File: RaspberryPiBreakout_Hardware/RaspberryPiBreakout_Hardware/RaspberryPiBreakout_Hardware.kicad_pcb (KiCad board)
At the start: 2 copper layers, 124.5 x 79.2 mm, 28 parts, among them U1 OKI, U2 Raspberry_Pi, U3 OKI

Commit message: layout and schematic changes
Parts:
- removed C2: 10u, Capacitor_SMD:C_0603_1608Metric_Pad1.05x0.95mm_HandSolder
- removed D2: LED, Diode_SMD:D_0603_1608Metric_Pad1.05x0.95mm_HandSolder
- removed G***: LOGO, MRDT_Silkscreens:0_MRDT_Logo_20mm
- removed R2: 500, Resistor_SMD:R_0603_1608Metric_Pad1.05x0.95mm_HandSolder
- removed U1: OKI, MRDT_Devices:OKI_Horizontal
- moved D1 3.81 mm to (156.4, 95.2)
- moved R1 3.81 mm to (151.4, 95.2)
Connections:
- U2 pad 2: +5V -> (no net)
- U2 pad 4: +5V -> (no net)
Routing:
- net +5V: track 57.5 -> 0.00 mm
- net +12V: track 98.4 -> 67.3 mm, vias 2 -> 0
- net SDA1: track 130.0 -> 135.0 mm, vias 6 -> 4
- net SCL1: track 117.5 -> 122.2 mm, vias 4 -> 5
- net Net-(D2-Pad2): track 3.17 -> 0.00 mm
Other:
- board text added: "3V3"
- board text added: "Raspberry Pi Breakout, Rev 1 Mars Rover Design Team Missouri S&T, 2020 Zak Brooks"
- board text added: "Rx"
- board text added: "Tx"
- board text removed: "5v"
- board text removed: "Raspberry Pi Breakout, Rev 2 Mars Rover Design Team Missouri S&T, 2019 Zak Brooks"

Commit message: finished updating layout
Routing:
- net +12V: track 67.3 -> 98.4 mm
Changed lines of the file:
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@@
     (thickness 1.6)
     (drawings 40)
-    (tracks 83)
+    (tracks 86)
     (zones 0)
     (modules 23)
@@
   (segment (start 112.395 102.87) (end 112.395 106.045) (width 0.762) (layer F.Cu) (net 2))
   (segment (start 112.395 102.87) (end 112.395 88.9) (width 0.762) (layer F.Cu) (net 2))
-  (segment (start 119.38 91.44) (end 119.38 106.045) (width 0.762) (layer F.Cu) (net 2))
   (segment (start 119.38 88.9) (end 119.38 91.44) (width 0.762) (layer F.Cu) (net 2))
+  (segment (start 149.87 95.25) (end 119.38 95.25) (width 0.381) (layer F.Cu) (net 2))
+  (segment (start 150.495 95.25) (end 149.87 95.25) (width 0.381) (layer F.Cu) (net 2))
+  (segment (start 119.38 91.44) (end 119.38 95.25) (width 0.762) (layer F.Cu) (net 2))
+  (segment (start 119.38 95.25) (end 119.38 106.045) (width 0.762) (layer F.Cu) (net 2))
   (segment (start 107.315 102.87) (end 107.315 106.045) (width 0.762) (layer F.Cu) (net 3))
   (segment (start 107.315 78.74) (end 107.315 83.185) (width 0.762) (layer B.Cu) (net 3))

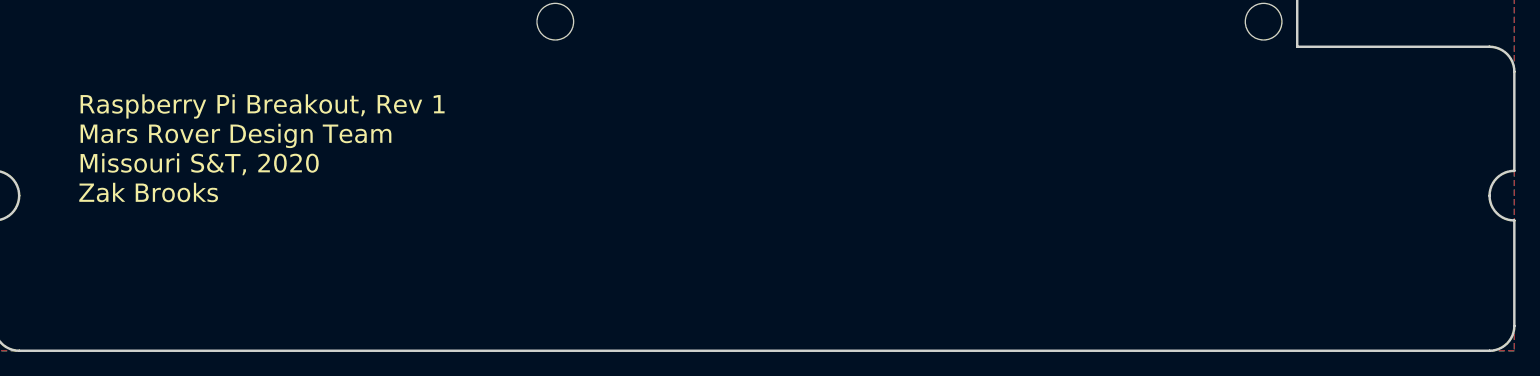
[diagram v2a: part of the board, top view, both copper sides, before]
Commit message: Added silkscreens
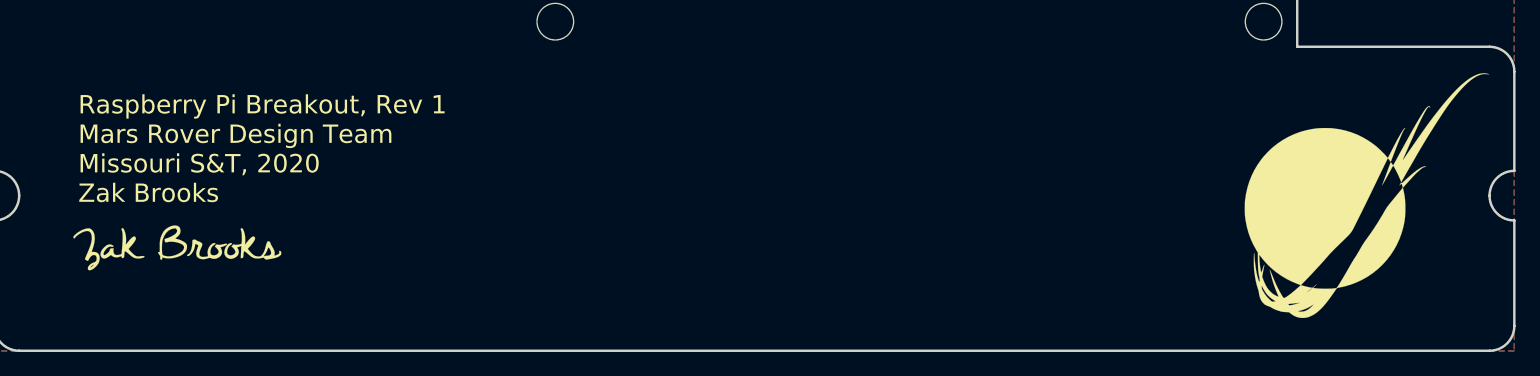
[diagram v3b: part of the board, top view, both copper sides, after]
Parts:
- added G***: LOGO, MRDT_Silkscreens:z_sig_ZakBrooks_sig15mm, F.Cu at (87.0, 145.4)
- added G***: LOGO, MRDT_Silkscreens:0_MRDT_Logo_20mm, F.Cu at (184.8, 141.0)
- added G***: LOGO, MRDT_Silkscreens:2_Dahlbot_2.0, B.Cu at (182.9, 142.2)

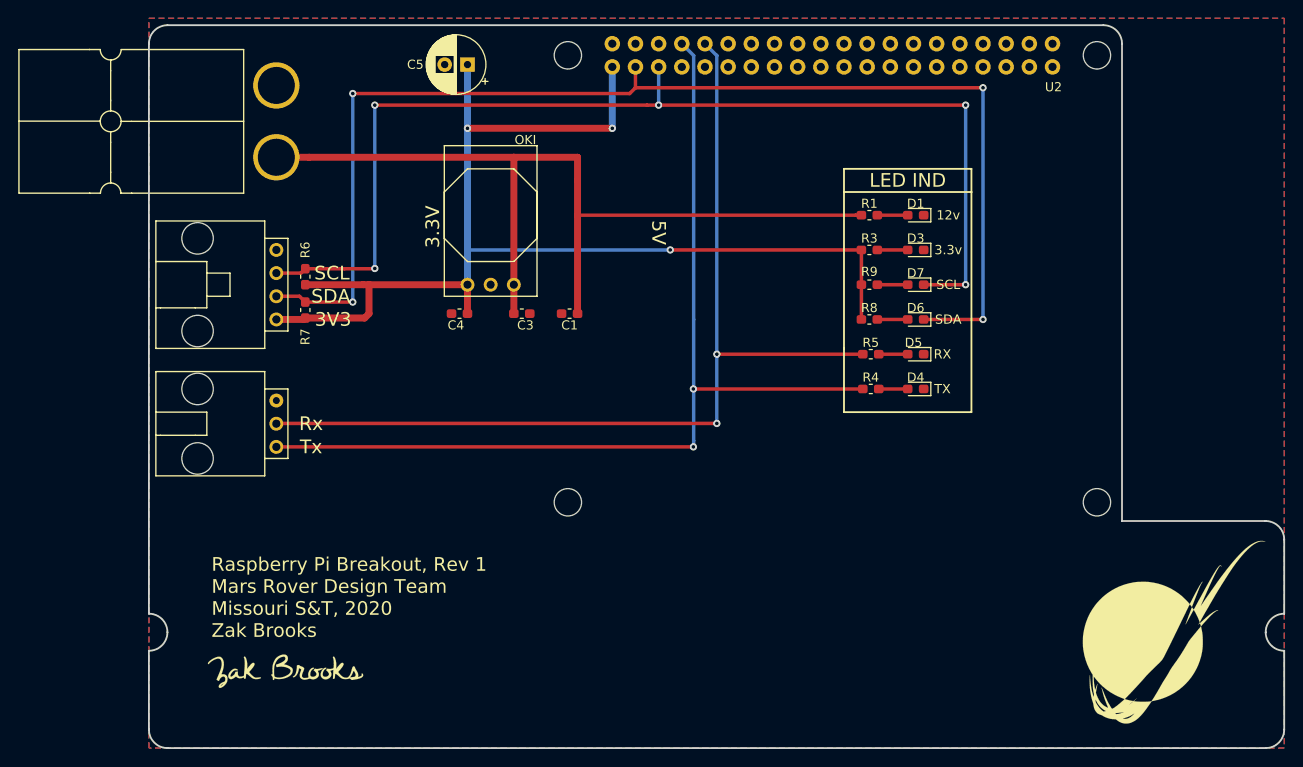
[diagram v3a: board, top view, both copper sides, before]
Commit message: Added 5v OKI back to the layout
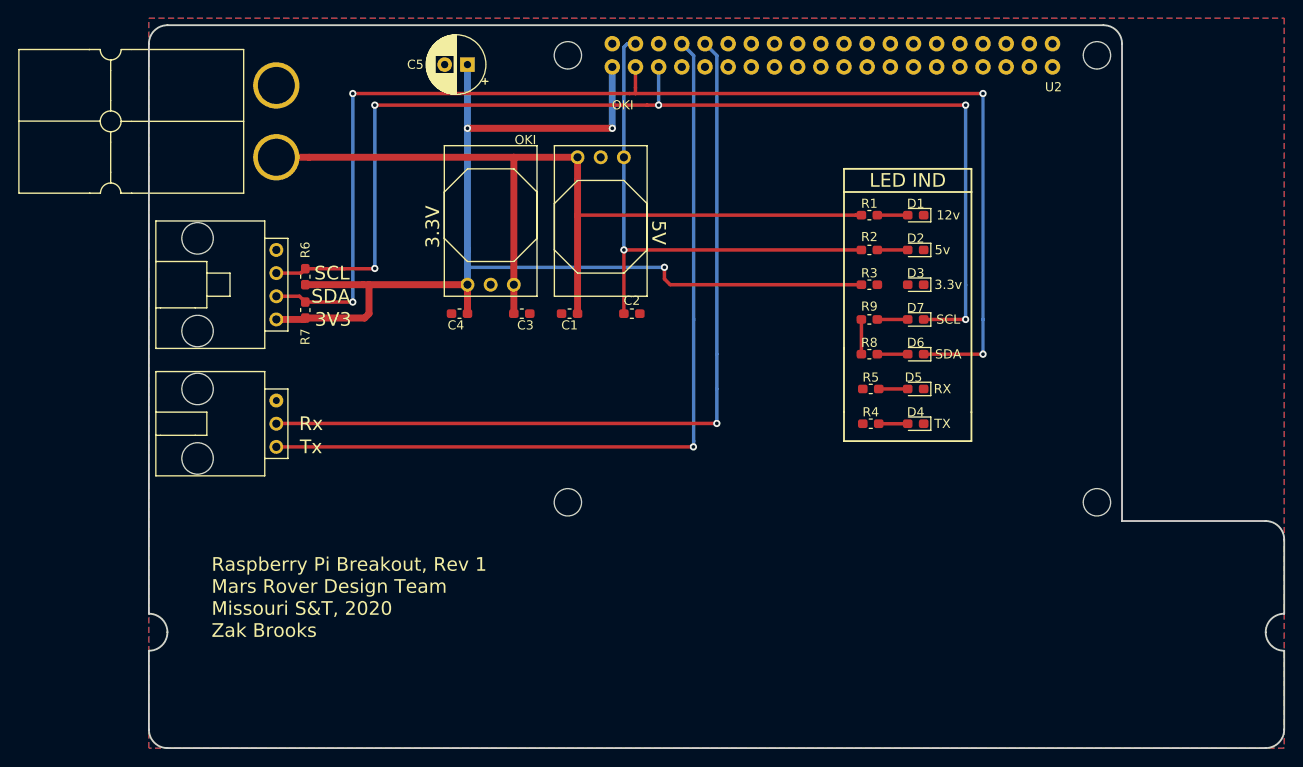
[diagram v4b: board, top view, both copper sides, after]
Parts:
- removed G***: LOGO, MRDT_Silkscreens:z_sig_ZakBrooks_sig15mm
- removed G***: LOGO, MRDT_Silkscreens:0_MRDT_Logo_20mm
- removed G***: LOGO, MRDT_Silkscreens:2_Dahlbot_2.0
- added C2: 10u, Capacitor_SMD:C_0603_1608Metric_Pad1.05x0.95mm_HandSolder, F.Cu at (125.3, 106.0)
- added D2: LED, Diode_SMD:D_0603_1608Metric_Pad1.05x0.95mm_HandSolder, F.Cu at (156.4, 99.1)
- added R2: 500, Resistor_SMD:R_0603_1608Metric_Pad1.05x0.95mm_HandSolder, F.Cu at (151.4, 99.1)
- added U1: OKI, MRDT_Devices:OKI_Horizontal, F.Cu at (116.8, 87.6)
- moved D3 3.81 mm to (156.4, 102.9)
- moved D4 3.81 mm to (156.4, 118.1)
- moved D5 3.81 mm to (156.4, 114.3)
- moved D7 3.81 mm to (156.4, 106.7)
- moved R3 3.81 mm to (151.4, 102.9)
- moved R4 3.81 mm to (151.5, 118.1)
- moved R5 3.81 mm to (151.5, 114.3)
- moved R9 3.81 mm to (151.4, 106.7)
- moved D6 3.81 mm to (156.4, 110.5)
- moved R8 3.81 mm to (151.4, 110.5)
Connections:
- U2 pad 2: (no net) -> +5V
- U2 pad 4: (no net) -> +5V
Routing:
- net +5V: track 0.00 -> 56.7 mm, vias 0 -> 1
- net Serial_Tx: track 109.0 -> 90.5 mm, vias 2 -> 1
- net Serial_Rx: track 106.5 -> 90.5 mm, vias 2 -> 1
- net SCL1: track 122.2 -> 126.0 mm
- net SDA1: track 135.0 -> 138.6 mm
- net Net-(D2-Pad2): track 0.00 -> 3.33 mm
- net Net-(D3-Pad2): track 3.17 -> 0.00 mm
- net +3V3: track 132.2 -> 129.8 mm
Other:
- board text added: "5v"

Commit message: Wired up
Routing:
- net Serial_Tx: track 90.5 -> 110.5 mm, vias 1 -> 2
- net Serial_Rx: track 90.5 -> 106.5 mm, vias 1 -> 2
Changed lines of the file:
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@@
     (thickness 1.6)
     (drawings 43)
-    (tracks 95)
+    (tracks 102)
     (zones 0)
     (modules 27)
@@
   (segment (start 107.315 100.965) (end 107.315 102.87) (width 0.762) (layer B.Cu) (net 3))
   (segment (start 107.315 99.06) (end 107.315 100.965) (width 0.762) (layer B.Cu) (net 3))
-  (via (at 128.905 100.965) (size 0.8) (drill 0.4) (layers F.Cu B.Cu) (net 3))
-  (segment (start 128.905 102.235) (end 128.905 100.965) (width 0.381) (layer F.Cu) (net 3))
-  (segment (start 129.54 102.87) (end 128.905 102.235) (width 0.381) (layer F.Cu) (net 3))
   (segment (start 150.495 102.87) (end 129.54 102.87) (width 0.381) (layer F.Cu) (net 3))
   (segment (start 107.315 100.965) (end 128.905 100.965) (width 0.381) (layer B.Cu) (net 3))
+  (segment (start 128.905 100.965) (end 129.54 101.6) (width 0.381) (layer B.Cu) (net 3))
+  (via (at 129.54 102.87) (size 0.8) (drill 0.4) (layers F.Cu B.Cu) (net 3))
+  (segment (start 129.54 101.6) (end 129.54 102.87) (width 0.381) (layer B.Cu) (net 3))
   (segment (start 130.81 76.454) (end 132.109499 77.753499) (width 0.381) (layer B.Cu) (net 4))
   (via (at 132.08 120.65) (size 0.8) (drill 0.4) (layers F.Cu B.Cu) (net 4))
@@
   (segment (start 132.109499 77.753499) (end 132.109499 106.68) (width 0.381) (layer B.Cu) (net 4))
   (segment (start 132.109499 106.68) (end 132.109499 119.985501) (width 0.381) (layer B.Cu) (net 4))
+  (segment (start 132.109499 119.985501) (end 136.554499 119.985501) (width 0.381) (layer B.Cu) (net 4))
+  (via (at 137.16 118.11) (size 0.8) (drill 0.4) (layers F.Cu B.Cu) (net 4))
+  (segment (start 136.554499 119.985501) (end 137.16 119.38) (width 0.381) (layer B.Cu) (net 4))
+  (segment (start 137.16 119.38) (end 137.16 118.11) (width 0.381) (layer B.Cu) (net 4))
+  (segment (start 137.16 118.11) (end 150.65 118.11) (width 0.381) (layer F.Cu) (net 4))
   (segment (start 133.35 76.454) (end 134.649499 77.753499) (width 0.381) (layer B.Cu) (net 5))
   (via (at 134.649499 118.080501) (size 0.8) (drill 0.4) (layers F.Cu B.Cu) (net 5))
@@
   (segment (start 134.649499 110.49) (end 134.649499 114.3) (width 0.381) (layer B.Cu) (net 5))
   (segment (start 134.649499 114.3) (end 134.649499 118.080501) (width 0.381) (layer B.Cu) (net 5))
+  (via (at 134.649499 114.3) (size 0.8) (drill 0.4) (layers F.Cu B.Cu) (net 5))
+  (segment (start 150.65 114.3) (end 134.649499 114.3) (width 0.381) (layer F.Cu) (net 5))
   (segment (start 88.9 104.14) (end 89.535 104.775) (width 0.381) (layer F.Cu) (net 6))
   (segment (start 86.36 104.14) (end 88.9 104.14) (width 0.381) (layer F.Cu) (net 6))

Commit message: Layout differences?
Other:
- board text added: "-"
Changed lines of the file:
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@@
   (general
     (thickness 1.6)
-    (drawings 43)
+    (drawings 45)
     (tracks 102)
     (zones 0)
@@
   )
   (setup
-    (last_trace_width 0.381)
+    (last_trace_width 0.25)
     (user_trace_width 0.381)
     (user_trace_width 0.762)
@@
     )
   )
+  (gr_text - (at 92.075 99.06) (layer F.SilkS)
+    (effects (font (size 1.5 1.5) (thickness 0.3)))
+  )
+  (gr_text - (at 90.17 115.57) (layer F.SilkS)
+    (effects (font (size 1.5 1.5) (thickness 0.3)))
+  )
   (gr_line (start 148.59 120.015) (end 148.59 116.84) (layer F.SilkS) (width 0.2))

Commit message: Theoretically done board
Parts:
- added C6: 680uF, Capacitor_THT:CP_Radial_D6.3mm_P2.50mm, F.Cu at (97.5, 81.0)
- added Conn4: Molex_SL_04, MRDT_Connectors:MOLEX_SL_04_Horizontal, F.Cu at (86.1, 103.6)
- added R10: 4.7k, Resistor_SMD:R_0603_1608Metric_Pad1.05x0.95mm_HandSolder, F.Cu at (89.5, 99.8)
- added R11: 4.7k, Resistor_SMD:R_0603_1608Metric_Pad1.05x0.95mm_HandSolder, F.Cu at (89.5, 102.4)
- C5: value CP1 -> 680uF
- R2, R4, R5: value 500 -> 510
- R3, R8, R9: value 500 -> 330
- moved Conn1 83.3 mm to (164.5, 109.0), turned to 180 degrees
- moved C4 62.2 mm to (168.7, 106.3), turned to 270 degrees
- moved C3 55.7 mm to (168.5, 99.5), turned to 90 degrees
- moved U3 53.1 mm to (167.6, 97.8), turned to 270 degrees
- moved C1 52.8 mm to (168.9, 90.3), turned to 270 degrees
- moved C2 49.1 mm to (168.9, 83.5), turned to 90 degrees
- moved C5 43.9 mm to (143.1, 104.1), turned to 90 degrees
- moved R1 42.2 mm to (109.2, 93.5)
- moved R2 42.2 mm to (109.2, 97.3)
- moved R3 42.2 mm to (109.2, 101.1)
- moved R4 42.2 mm to (109.4, 116.3)
- moved R5 42.2 mm to (109.4, 112.5)
- moved R8 42.2 mm to (109.2, 108.7)
- moved R9 42.2 mm to (109.2, 104.9)
- moved D1 42.2 mm to (114.3, 93.5)
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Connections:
- Conn3 pad 2: SDA1 -> GND
- Conn3 pad 3: SCL1 -> SDA1
- Conn3 pad 4: GND -> SCL1
- U2 pad 1: +3V3 -> (no net)
- U2 pad 17: +3V3 -> (no net)
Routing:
- net +5V: track 56.7 -> 93.7 mm, vias 1 -> 4
- net +3V3: track 129.8 -> 150.8 mm, vias 3 -> 4
- net Serial_Tx: track 110.5 -> 92.5 mm
- net SDA1: track 138.6 -> 124.6 mm
- net Serial_Rx: track 106.5 -> 96.6 mm
- net +12V: track 98.4 -> 92.5 mm, vias 0 -> 1
- net Net-(D3-Pad2): track 0.00 -> 3.33 mm
- net SCL1: track 126.0 -> 128.5 mm, vias 5 -> 4
- net GND: vias 0 -> 7
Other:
- board text added: "Raspberry Pi Breakout, Rev 2 Mars Rover Design Team Missouri S&T, 2020 Zak Brooks"
- board text removed: "Raspberry Pi Breakout, Rev 1 Mars Rover Design Team Missouri S&T, 2020 Zak Brooks"

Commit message: Added silkscreens
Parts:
- added G***: LOGO, MRDT_Silkscreens:z_sig_ZakBrooks_sig15mm, F.Cu at (87.6, 144.8)
- added G***: LOGO, MRDT_Silkscreens:0_MRDT_Logo_20mm, F.Cu at (181.6, 141.0)
- added G***: LOGO, MRDT_Silkscreens:2_Dahlbot_2.0, B.Cu at (85.1, 139.7)
- added G***: LOGO, MRDT_Silkscreens:2_Meh, B.Cu at (80.0, 81.3)
